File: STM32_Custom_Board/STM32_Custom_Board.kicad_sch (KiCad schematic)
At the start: 1 part, among them U1 STM32F103C8T6

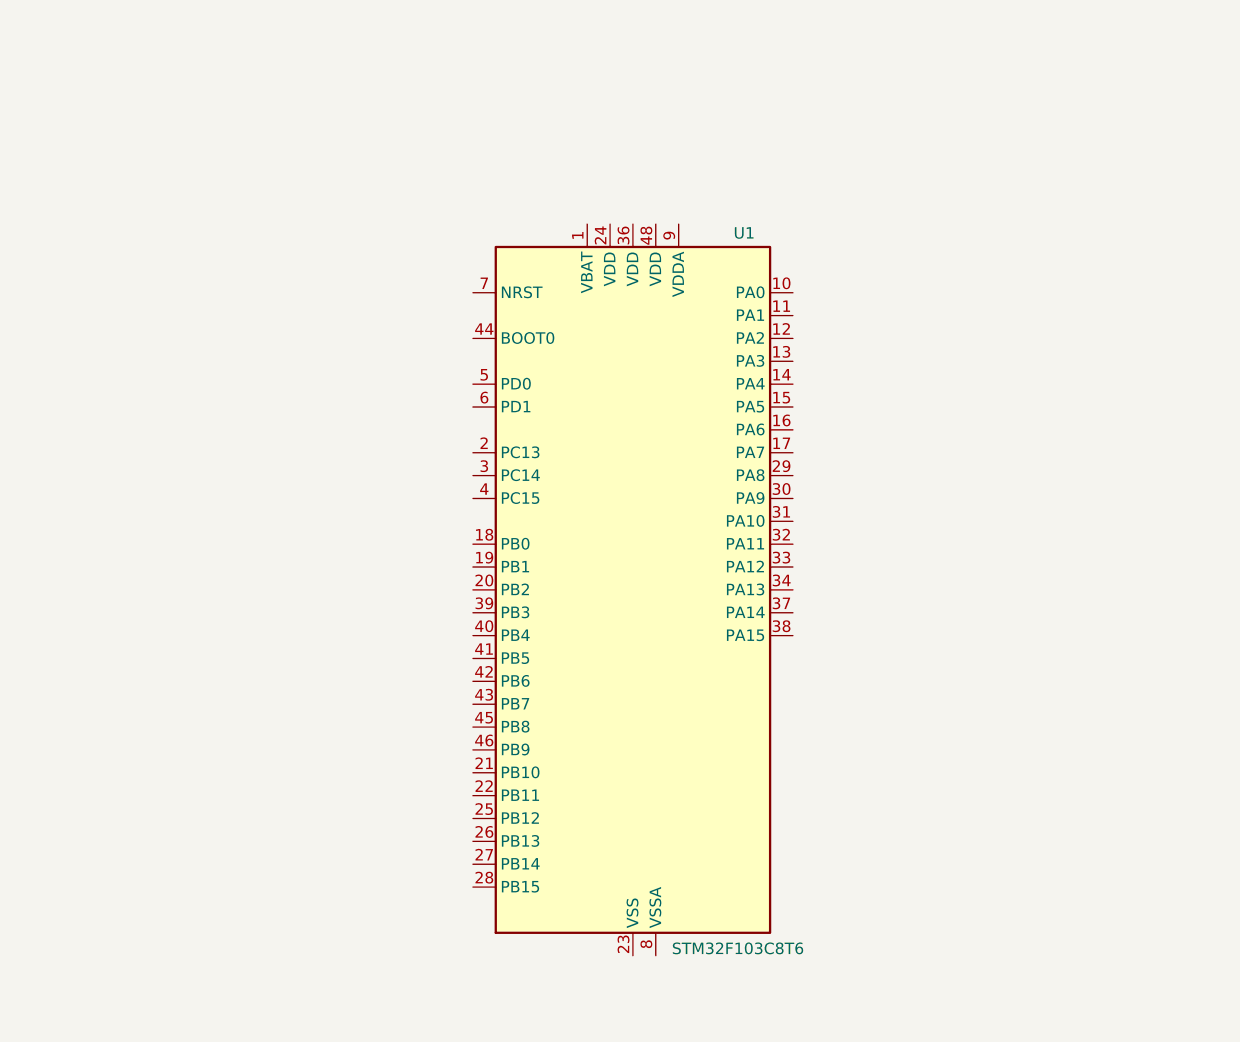
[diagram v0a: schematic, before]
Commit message: Decoupling capacitors for NRST and VDA added
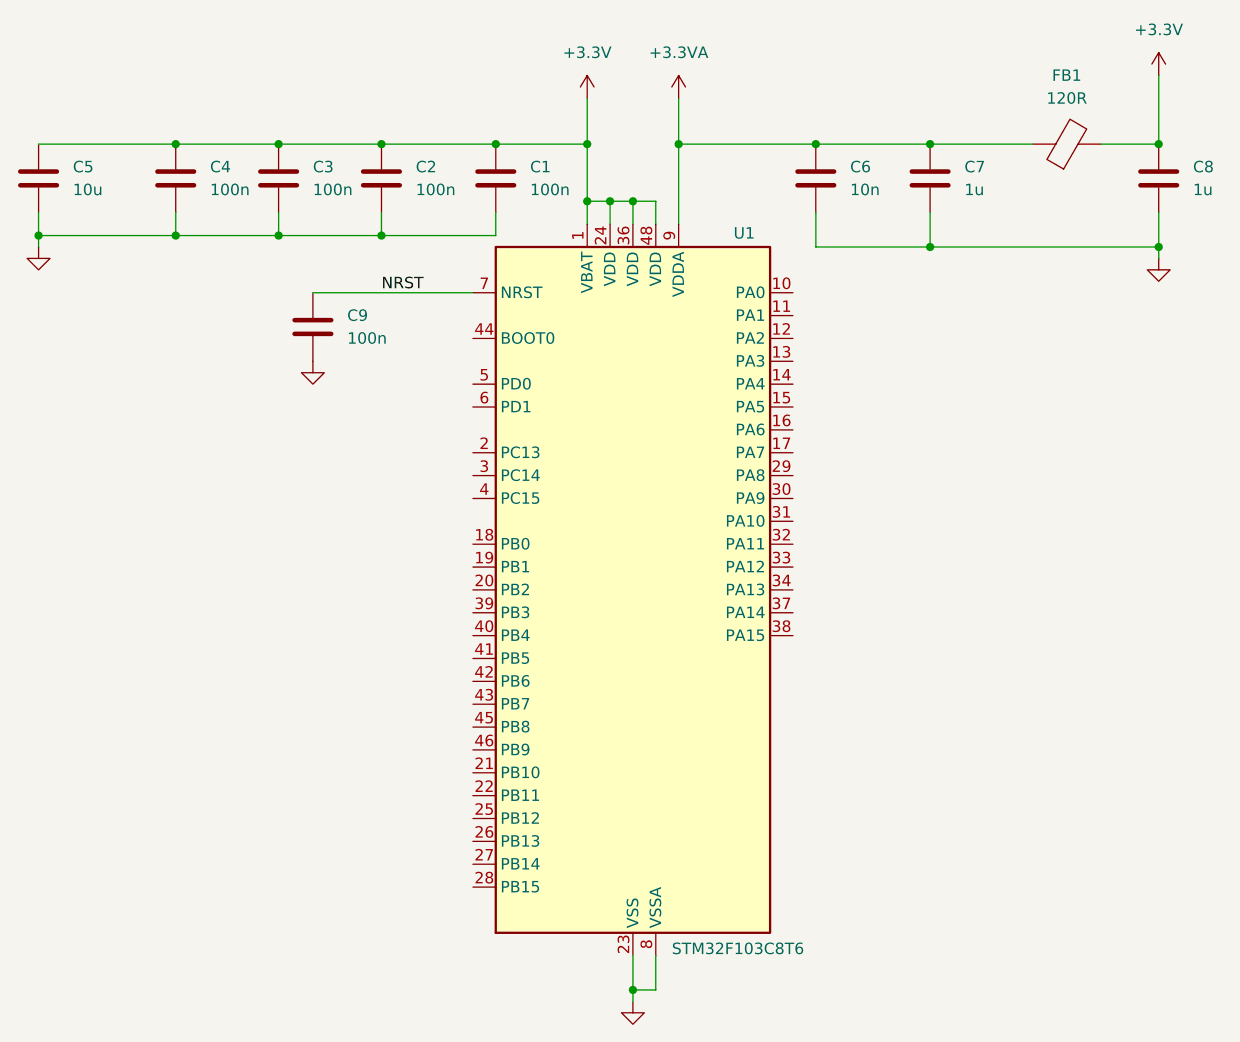
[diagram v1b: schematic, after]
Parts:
- added C1, C2, C3, C4, C9: 100n, symbol Device:C
- added C5: 10u, symbol Device:C
- added C6: 10n, symbol Device:C
- added C7, C8: 1u, symbol Device:C
- added FB1: 120R, symbol Device:FerriteBead
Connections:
- net +3.3V: now reaches U1.1 (VBAT)
- net +3.3V: now also U1.24 (VDD), U1.36 (VDD), U1.48 (VDD), C1.1, C2.1, C3.1, C4.1, C5.1, C8.1, FB1.2
- net GND: now reaches U1.23 (VSS), U1.35 (VSS), U1.47 (VSS)
- net GND: now also U1.8 (VSSA), C1.2, C2.2, C3.2, C4.2, C5.2, C6.2, C7.2, C8.2, C9.2
- net NRST: now reaches U1.7 (NRST)
- net NRST: now also C9.1
- net +3.3VA: now reaches U1.9 (VDDA)
- net +3.3VA: now also C6.1, C7.1, FB1.1

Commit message: Switch in boot pin added
Quartz Crystal added
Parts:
- added C10, C11: 10p, symbol Device:C
- added R1: 10k, symbol Device:R
- added SW1: SW_SPDT, symbol Switch:SW_SPDT
- added Y1: 16MHz, symbol Device:Crystal_GND24
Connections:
- net +3.3V: now also SW1.1 (A)
- net GND: now also C10.2, C11.2, SW1.3 (C), Y1.2, Y1.4
- net USB_D-: now reaches U1.31 (PA10)
- net USB_D+: now reaches U1.32 (PA11)
- net SWDIO: now reaches U1.33 (PA12)
- net SWCLK: now reaches U1.34 (PA13)
- net BOOT0: now reaches U1.44 (BOOT0)
- net BOOT0: now also R1.2
- net HSE_IN: now reaches U1.5 (PD0)
- net HSE_IN: now also C11.1, Y1.1
- net HSE_OUT: now reaches U1.6 (PD1)
- net HSE_OUT: now also C10.1, Y1.3
- new net SW_BOOT0: R1.1, SW1.2 (B)
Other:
- moved on the sheet: C9

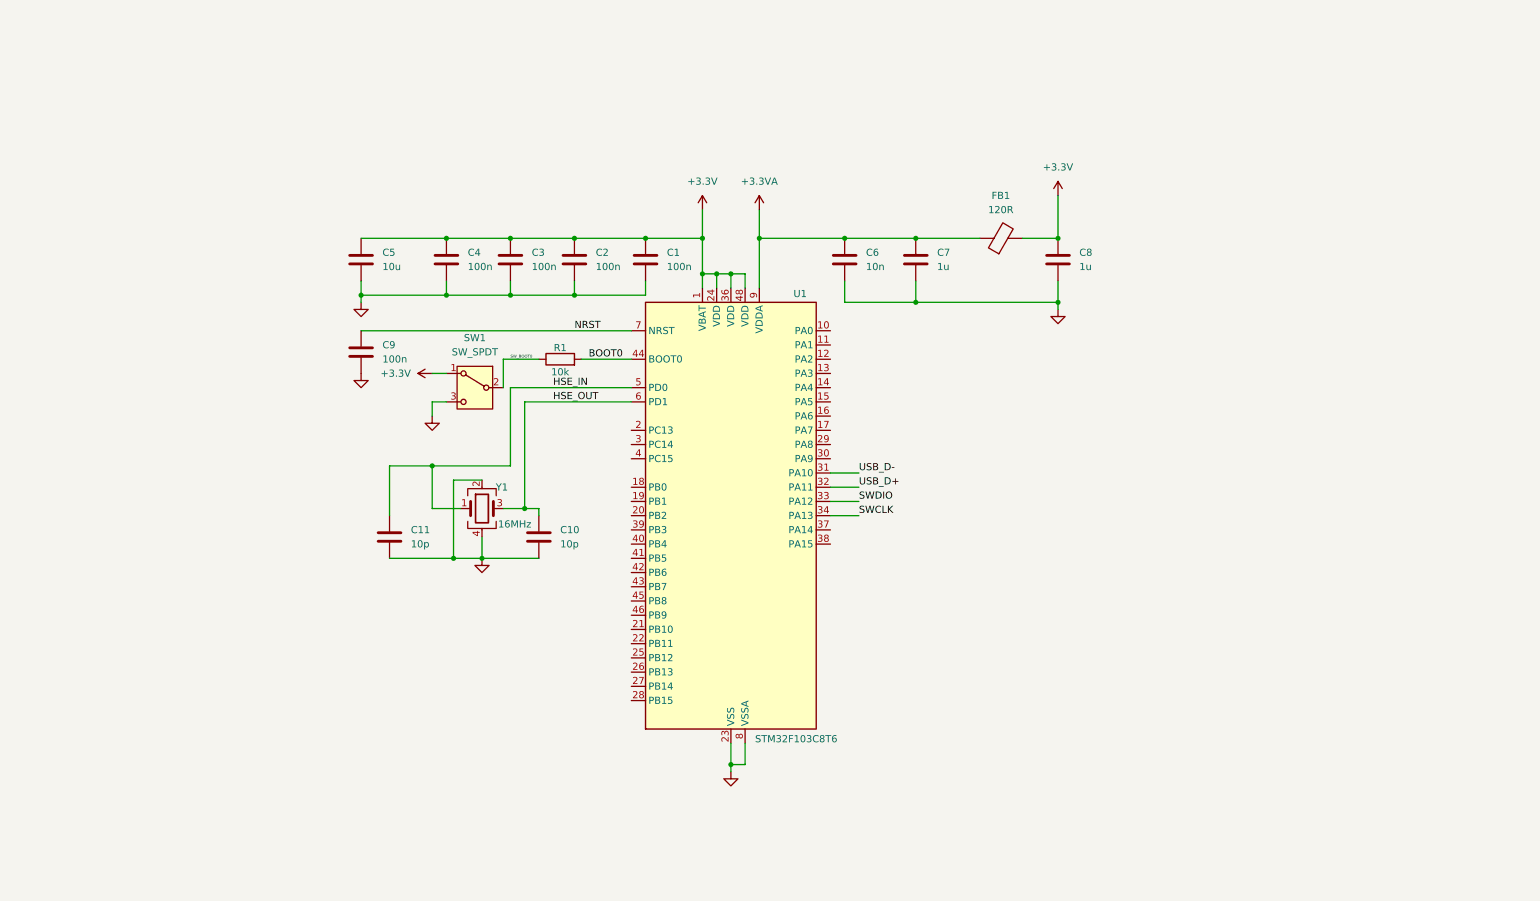
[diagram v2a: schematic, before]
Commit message: micro USB B added
Serial debugging connections added

UART connections added

I2C connections added

Power supply LDO added
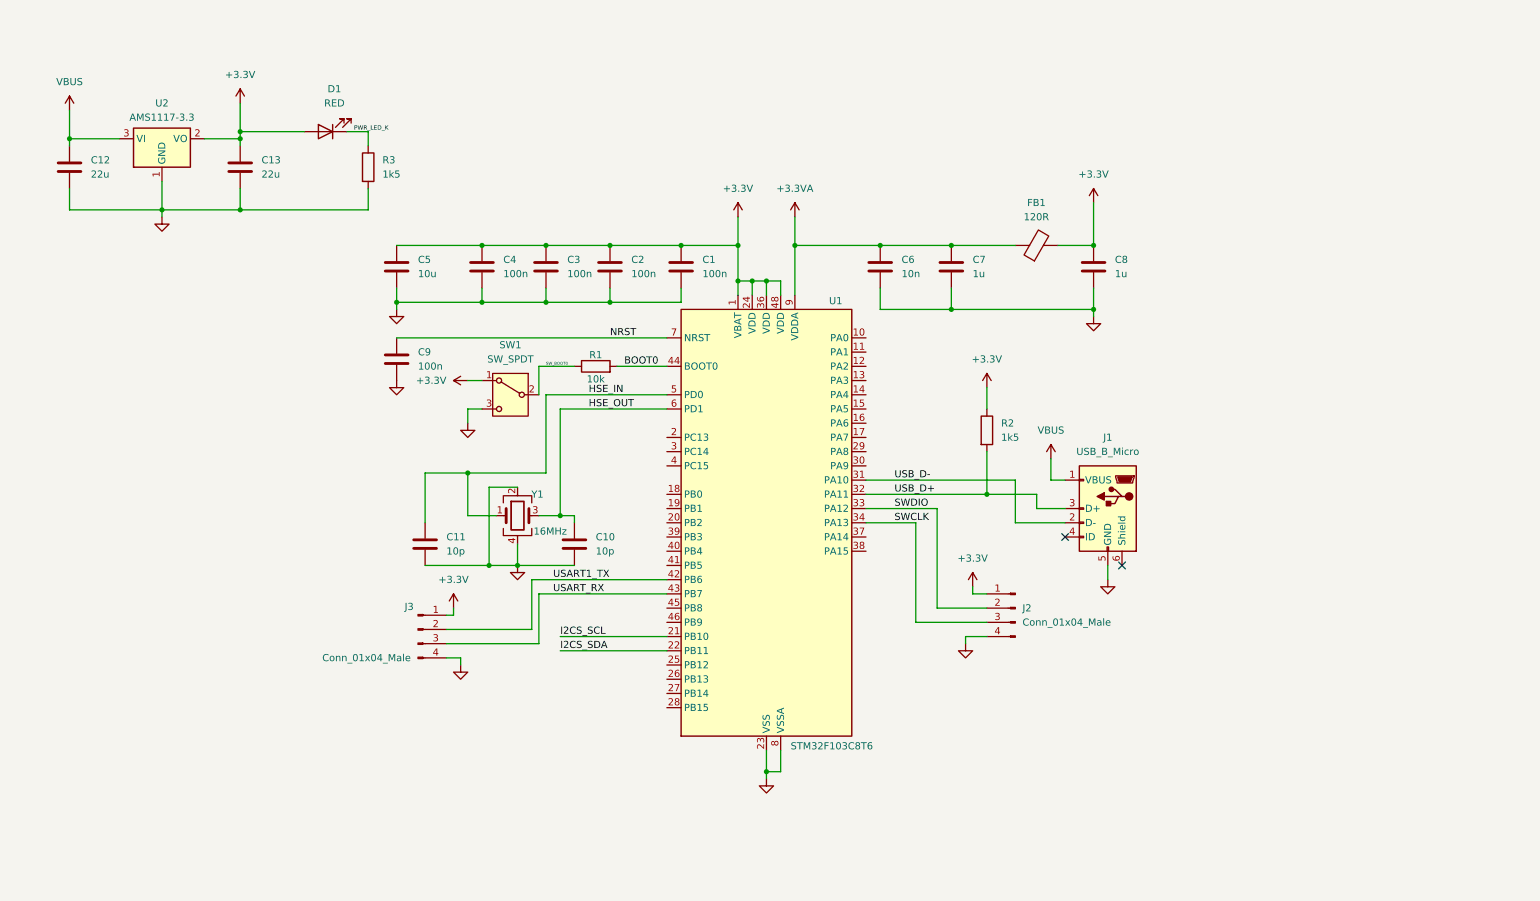
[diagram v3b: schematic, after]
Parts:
- added C12, C13: 22u, symbol Device:C
- added D1: RED, symbol Device:LED
- added J1: USB_B_Micro, symbol Connector:USB_B_Micro
- added J2, J3: Conn_01x04_Male, symbol Connector:Conn_01x04_Pin
- added R2, R3: 1k5, symbol Device:R
- added U2: AMS1117-3.3, Package_TO_SOT_SMD:SOT-223-3_TabPin2, symbol Regulator_Linear:AMS1117-3.3
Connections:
- net +3.3V: now also C13.1, D1.2 (A), J2.1 (Pin_1), J3.1 (Pin_1), R2.1, U2.2 (VO)
- net GND: now also C12.2, C13.2, J1.5 (GND), J2.4 (Pin_4), J3.4 (Pin_4), R3.2, U2.1 (GND)
- net SWCLK: now also J2.3 (Pin_3)
- net SWDIO: now also J2.2 (Pin_2)
- net USB_D+: now also J1.3 (D+), R2.2
- net USB_D-: now also J1.2 (D-)
- net I2CS_SCL: now reaches U1.21 (PB10)
- net I2CS_SDA: now reaches U1.22 (PB11)
- net USART1_TX: now reaches U1.42 (PB6)
- net USART1_TX: now also J3.2 (Pin_2)
- net USART_RX: now reaches U1.43 (PB7)
- net USART_RX: now also J3.3 (Pin_3)
- new net PWR_LED_K: D1.1 (K), R3.1
- new net VBUS: C12.1, J1.1 (VBUS), U2.3 (VI)
- no-connect marks 0 -> 2
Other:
- moved on the sheet: C1, C10, C11, C2, C3, C4, C5, C6, C7, C8, C9, FB1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

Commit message: Schematic polished and finished
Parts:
- added J4: Conn_01x04_Male, symbol Connector:Conn_01x04_Pin
- added R4, R5: 1k5, symbol Device:R
- renumbered C12 to C1, C8 to C10, C9 to C11, C11 to C12, C10 to C13, C13 to C2, C5 to C3, C3 to C5, C2 to C6, C1 to C7, C6 to C8, C7 to C9, R3 to R1, R1 to R2, R2 to R3, U2 to U1, U1 to U2
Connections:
- net +3.3V: now also J4.1 (Pin_1), R4.1, R5.1
- net GND: now also J4.4 (Pin_4)
- net I2CS_SCL: now also J4.2 (Pin_2), R4.2
- net I2CS_SDA: now also J4.3 (Pin_3), R5.2
- no-connect marks 2 -> 29
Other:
- note added: "1 x 100 nF per VDD pin"
- note added: "CL=2*(CL0 = Cs)= 2 * (10 - 5)pF = 10pF"
- note added: "Microcontroller and USB"
- note added: "Pin-out using STM32CubeIDE"
- note added: "Power supply"
- note added: "STM32-BareBlue"
- note added: "USB App note AN4879"
- note added: "VBUS from USB connector(nom +5V) Min. 22uF inp/outp caps"
- note added: "VDDA filtering"
- company: (none) -> JLJV14-GITHUB
- title: (none) -> STM32-BareBlue
- moved on the sheet: C1, C10, C11, C12, C13, C2, C3, C4, C5, C6, C7, C8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

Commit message: Footprints assigned
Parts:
- C1, C2: footprint (none) -> Capacitor_SMD:C_0805_2012Metric
- C10, C11, C12, C13, C4, C5, C6, C7, C8, C9: footprint (none) -> Capacitor_SMD:C_0402_1005Metric
- C3: footprint (none) -> Capacitor_SMD:C_0603_1608Metric
- D1: footprint (none) -> LED_SMD:LED_0603_1608Metric
- FB1: footprint (none) -> Inductor_SMD:L_0603_1608Metric
- J1: footprint (none) -> Connector_USB:USB_Micro-B_Wuerth_629105150521
- J2, J3, J4: footprint (none) -> Connector_PinHeader_2.54mm:PinHeader_1x04_P2.54mm_Vertical
- R1, R2, R3, R4, R5: footprint (none) -> Resistor_SMD:R_0402_1005Metric
- SW1: footprint (none) -> Button_Switch_THT:SW_E-Switch_EG1224_SPDT_Angled
- Y1: footprint (none) -> Crystal:Crystal_SMD_3225-4Pin_3.2x2.5mm_HandSoldering
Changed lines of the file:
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@@
 			)
 		)
-		(property "Footprint" ""
+		(property "Footprint" "Button_Switch_THT:SW_E-Switch_EG1224_SPDT_Angled"
 			(at 165.1 77.47 0)
 			(effects
@@
 			)
 		)
-		(property "Footprint" ""
+		(property "Footprint" "Resistor_SMD:R_0402_1005Metric"
 			(at 75.692 52.07 90)
 			(effects
@@
 			)
 		)
-		(property "Footprint" ""
+		(property "Footprint" "Capacitor_SMD:C_0603_1608Metric"
 			(at 145.7452 58.42 0)
 			(effects
@@
 			)
 		)
-		(property "Footprint" ""
+		(property "Footprint" "Resistor_SMD:R_0402_1005Metric"
 			(at 153.162 140.97 90)
 			(effects
@@
 			)
 		)
-		(property "Footprint" ""
+		(property "Footprint" "Resistor_SMD:R_0402_1005Metric"
 			(at 248.412 83.82 90)
 			(effects
@@
 			)
 		)
-		(property "Footprint" ""
+		(property "Footprint" "Connector_USB:USB_Micro-B_Wuerth_629105150521"
 			(at 267.97 99.06 0)
 			(effects
@@
 			)
 		)
-		(property "Footprint" ""
+		(property "Footprint" "Capacitor_SMD:C_0402_1005Metric"
 			(at 150.8252 107.95 0)
 			(effects
@@
 			)
 		)
-		(property "Footprint" ""
+		(property "Footprint" "Inductor_SMD:L_0603_1608Metric"
 			(at 259.08 52.578 90)
 			(effects
@@
 			)
 		)
-		(property "Footprint" ""
+		(property "Footprint" "Resistor_SMD:R_0402_1005Metric"
 			(at 144.272 140.97 90)
 			(effects
@@
 			)
 		)
-		(property "Footprint" ""
+		(property "Footprint" "Connector_PinHeader_2.54mm:PinHeader_1x04_P2.54mm_Vertical"
 			(at 127 148.59 0)
 			(effects
@@
 			)
 		)
-		(property "Footprint" ""
+		(property "Footprint" "Connector_PinHeader_2.54mm:PinHeader_1x04_P2.54mm_Vertical"
 			(at 148.59 119.38 0)
 			(effects
@@
 			)
 		)
-		(property "Footprint" ""
+		(property "Footprint" "Capacitor_SMD:C_0402_1005Metric"
 			(at 244.8052 58.42 0)
 			(effects
@@
 			)
 		)
-		(property "Footprint" ""
+		(property "Footprint" "Capacitor_SMD:C_0402_1005Metric"
 			(at 160.9852 58.42 0)
 			(effects
@@
 			)
 		)
-		(property "Footprint" ""
+		(property "Footprint" "Capacitor_SMD:C_0402_1005Metric"
 			(at 183.8452 58.42 0)
 			(effects
@@
 			)
 		)
-		(property "Footprint" ""
+		(property "Footprint" "Capacitor_SMD:C_0402_1005Metric"
 			(at 232.1052 58.42 0)
 			(effects
@@
 			)
 		)
-		(property "Footprint" ""
+		(property "Footprint" "Capacitor_SMD:C_0805_2012Metric"
 			(at 25.0952 55.88 0)
 			(effects
@@
 			)
 		)
-		(property "Footprint" ""
+		(property "Footprint" "Capacitor_SMD:C_0402_1005Metric"
 			(at 196.5452 58.42 0)
 			(effects
@@
 			)
 		)
-		(property "Footprint" ""
+		(property "Footprint" "Resistor_SMD:R_0402_1005Metric"
 			(at 180.34 74.168 90)
 			(effects
@@
 			)
 		)
-		(property "Footprint" ""
+		(property "Footprint" "Capacitor_SMD:C_0805_2012Metric"
 			(at 55.5752 55.88 0)
 			(effects
@@
 			)
 		)
-		(property "Footprint" ""
+		(property "Footprint" "Connector_PinHeader_2.54mm:PinHeader_1x04_P2.54mm_Vertical"
 			(at 255.27 115.57 0)
 			(effects
@@
 			)
 		)
-		(property "Footprint" ""
+		(property "Footprint" "Crystal:Crystal_SMD_3225-4Pin_3.2x2.5mm_HandSoldering"
 			(at 166.37 99.06 0)
 			(effects
@@
 			)
 		)
-		(property "Footprint" ""
+		(property "Footprint" "LED_SMD:LED_0603_1608Metric"
 			(at 69.85 45.72 0)
 			(effects
@@
 			)
 		)
-		(property "Footprint" ""
+		(property "Footprint" "Capacitor_SMD:C_0402_1005Metric"
 			(at 270.2052 58.42 0)
 			(effects
@@
 			)
 		)
-		(property "Footprint" ""
+		(property "Footprint" "Capacitor_SMD:C_0402_1005Metric"
 			(at 145.7452 74.93 0)
 			(effects
@@
 			)
 		)
-		(property "Footprint" ""
+		(property "Footprint" "Capacitor_SMD:C_0402_1005Metric"
 			(at 172.4152 58.42 0)
 			(effects
@@
 			)
 		)
-		(property "Footprint" ""
+		(property "Footprint" "Capacitor_SMD:C_0402_1005Metric"
 			(at 177.4952 107.95 0)
 			(effects
